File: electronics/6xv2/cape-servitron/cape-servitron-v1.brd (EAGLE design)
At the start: 158.8 x 147.3 mm, 104 parts, among them IC1 74541PW, IC2 74541PW, IC3 74541PW, IC4 LM2574M-5.0, M0-CONN PINHEAD-5MM-1X2, M0-CONN1 PINHEAD-5MM-1X2, M0-CONN2 PINHEAD-5MM-1X2, M0-CONN3 PINHEAD-5MM-1X2, M0-CONN4 PINHEAD-5MM-1X2, M0-CONN5 PINHEAD-5MM-1X2, Q1 BSS123

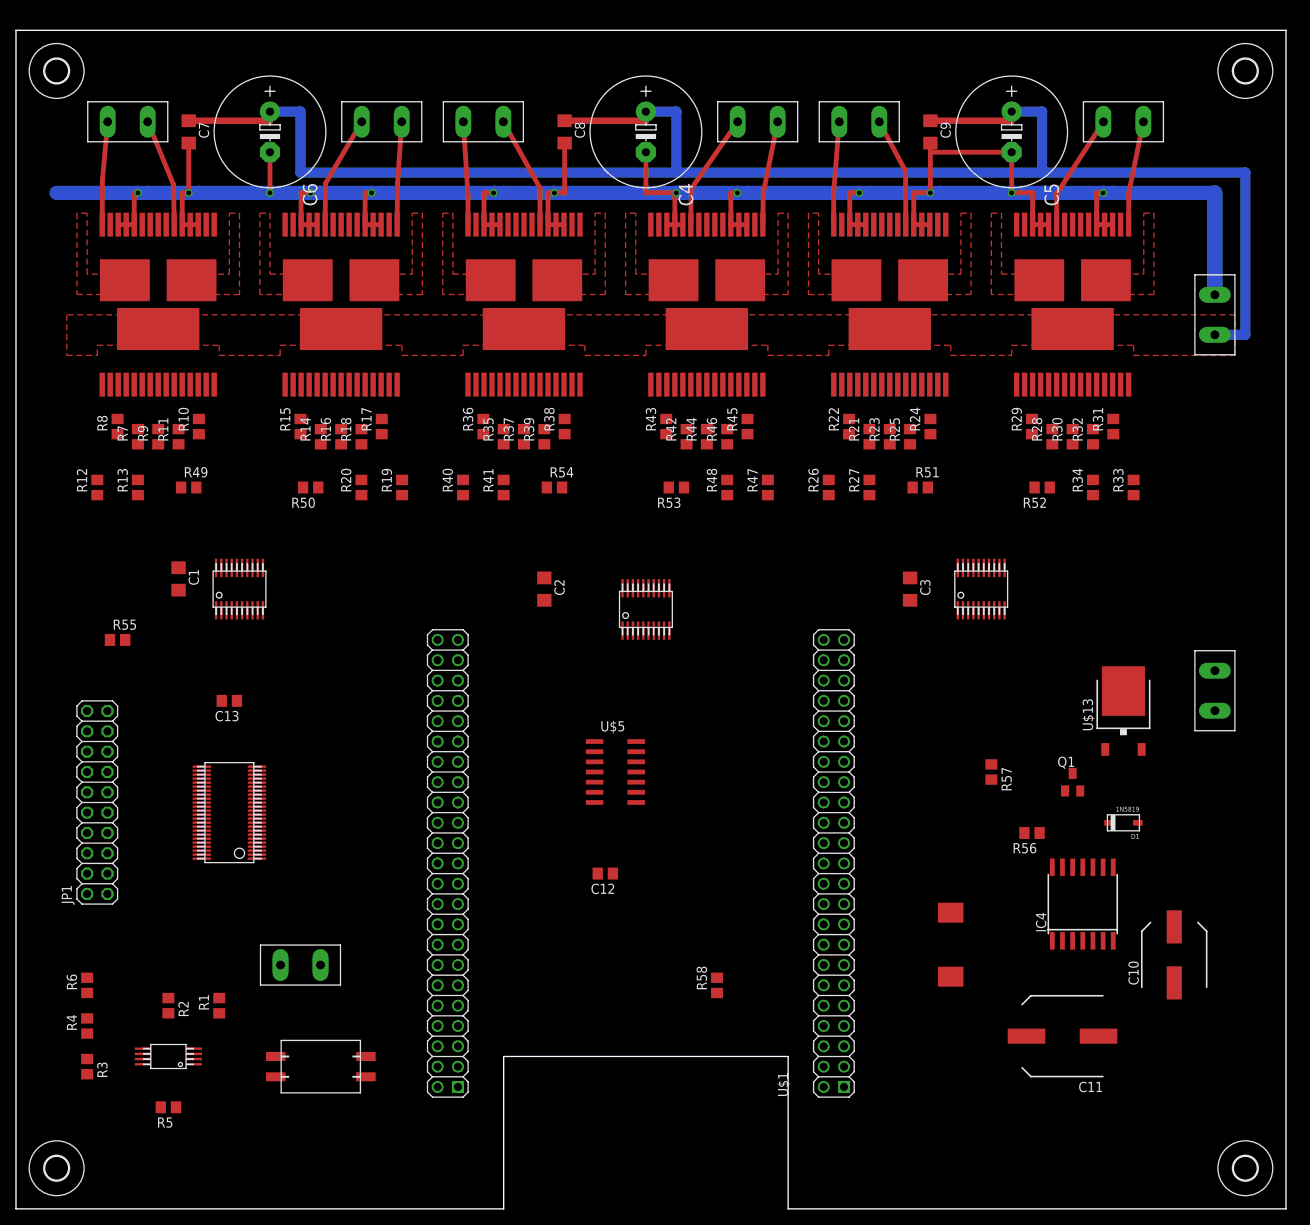
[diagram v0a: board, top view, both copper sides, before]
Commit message: added more heat sinking
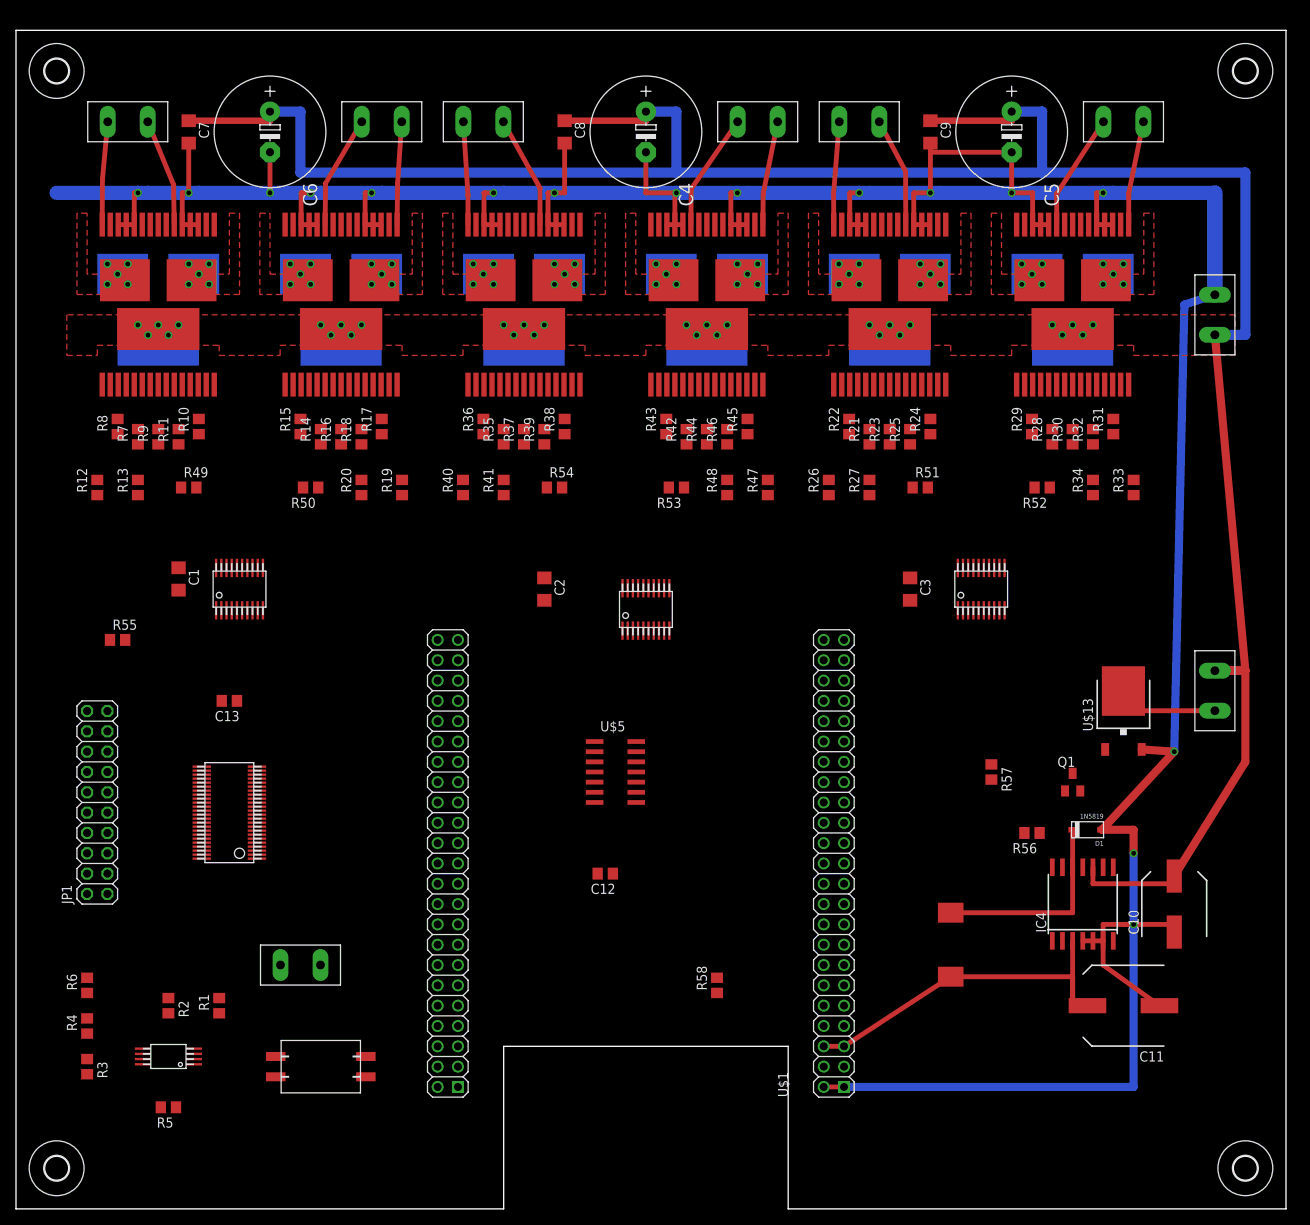
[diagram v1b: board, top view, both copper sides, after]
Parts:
- moved C11 8.52 mm to (138.4, 25.4)
- moved C10 6.35 mm to (144.8, 38.1)
- moved D1 4.56 mm to (133.9, 47.4)
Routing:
- net GND: track 308.9 -> 488.5 mm, vias 13 -> 16
- net +24V: track 210.4 -> 301.6 mm
- net VCC: track 0.00 -> 47.3 mm
- net N$26: track 0.00 -> 25.7 mm
- net N$27: track 0.00 -> 13.9 mm
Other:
- outline, holes or cut-outs redrawn

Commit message: board sent out; cleaning up quadrature assembly
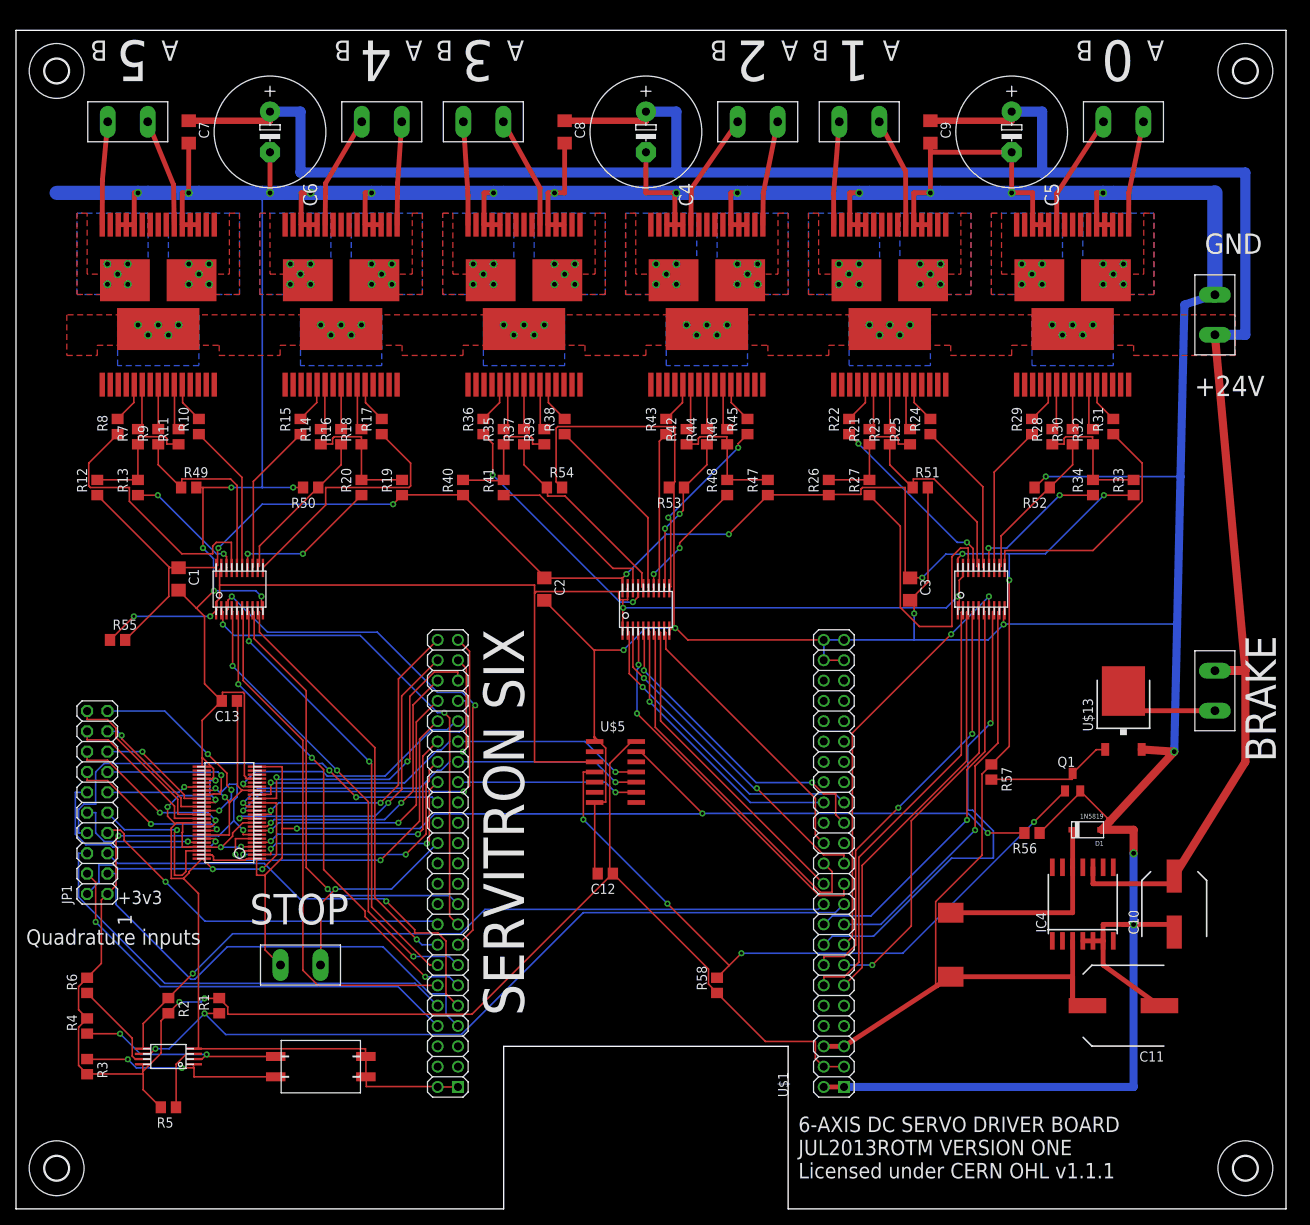
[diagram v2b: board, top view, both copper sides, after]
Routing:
- net GND: track 488.5 -> 980.2 mm, vias 16 -> 33
- net VCC: track 47.3 -> 283.1 mm, vias 0 -> 8
- net +3V3: track 0.00 -> 233.8 mm, vias 0 -> 6
- net !MALL-EN: track 0.00 -> 155.5 mm, vias 0 -> 4
- net EN_BUFFERS: track 0.00 -> 146.4 mm, vias 0 -> 3
- net I2C2_SCL: track 0.00 -> 99.4 mm, vias 0 -> 2
- net I2C2_SDA: track 0.00 -> 94.4 mm, vias 0 -> 1
- net BRAKE: track 0.00 -> 86.3 mm, vias 0 -> 4
- net M0-A: track 0.00 -> 68.9 mm, vias 0 -> 2
- net M1-EN: track 0.00 -> 65.8 mm
- net M0-EN: track 0.00 -> 61.3 mm, vias 0 -> 2
- net M0-B: track 0.00 -> 60.1 mm, vias 0 -> 3
- net M3-PWM: track 0.00 -> 59.7 mm, vias 0 -> 1
- net Q0-A: track 0.00 -> 58.8 mm
- net M0-PWM: track 0.00 -> 58.7 mm, vias 0 -> 3
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- added copper zone on layer 16, net +24V
- added copper zone on layer 16, net OUT0A
- added copper zone on layer 16, net OUT0B
- added copper zone on layer 16, net OUT1A
- added copper zone on layer 16, net OUT1B
- added copper zone on layer 16, net OUT2A
- added copper zone on layer 16, net OUT2B
- added copper zone on layer 16, net OUT3A
- added copper zone on layer 16, net OUT3B
- added copper zone on layer 16, net OUT4A
- added copper zone on layer 16, net OUT4B
- added copper zone on layer 16, net OUT5A
- added copper zone on layer 16, net OUT5B
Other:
- board text added: "+24V"
- board text added: "+3v3"
- board text added: "0"
- board text added: "1"
- board text added: "2"
- board text added: "3"
- board text added: "4"
- board text added: "5"
- board text added: "6-AXIS DC SERVO DRIVER BOARD JUL2013ROTM VERSION ONE Licensed under CERN OHL v1.1.1"
- board text added: "A"
- board text added: "B"
- board text added: "BRAKE"
- board text added: "GND"
- board text added: "Quadrature inputs"
- board text added: "SERVITRON SIX"
- board text added: "STOP"

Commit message: renamed chips and output signals to match board placement and markings
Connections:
- net OUT0A renamed OUT-5B
- net OUT0B renamed OUT-5A
- net OUT1A renamed OUT-4B
- net OUT1B renamed OUT-4A
- net OUT2A renamed OUT-1B
- net OUT2B renamed OUT-1A
- net OUT3A renamed OUT-0B
- net OUT3B renamed OUT-0A
- net OUT4A renamed OUT-3B
- net OUT4B renamed OUT-3A
- net OUT5A renamed OUT-2B
- net OUT5B renamed OUT-2A
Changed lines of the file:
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@@
 <wire x1="15.2908" y1="95.6564" x2="15.24" y2="95.57" width="0.2032" layer="1"/>
 </signal>
-<signal name="OUT0A" class="1">
+<signal name="OUT-5B" class="1">
 <contactref element="U$6" pad="P$1" route="any" routetag="OUT_A"/>
 <contactref element="U$6" pad="P$25" route="any" routetag="OUT_A"/>
@@
 </polygon>
 </signal>
-<signal name="OUT0B" class="1">
+<signal name="OUT-5A" class="1">
 <contactref element="U$6" pad="P$15" route="any" routetag="OUT_B"/>
 <contactref element="U$6" pad="P$16" route="any" routetag="OUT_B"/>
@@
 <wire x1="43.2308" y1="91.1352" x2="43.18" y2="91.12" width="0.2032" layer="1"/>
 </signal>
-<signal name="OUT1A" class="1">
+<signal name="OUT-4B" class="1">
 <contactref element="U$7" pad="P$1" route="any" routetag="OUT_A"/>
 <contactref element="U$7" pad="P$25" route="any" routetag="OUT_A"/>
@@
 </polygon>
 </signal>
-<signal name="OUT1B" class="1">
+<signal name="OUT-4A" class="1">
 <contactref element="U$7" pad="P$15" route="any" routetag="OUT_B"/>
 <contactref element="U$7" pad="P$16" route="any" routetag="OUT_B"/>
@@
 <wire x1="106.7308" y1="95.6564" x2="106.68" y2="95.57" width="0.2032" layer="1"/>
 </signal>
-<signal name="OUT2A" class="1">
+<signal name="OUT-1B" class="1">
 <contactref element="U$8" pad="P$1" route="any" routetag="OUT_A"/>
 <contactref element="U$8" pad="P$25" route="any" routetag="OUT_A"/>
@@
 </polygon>
 </signal>
-<signal name="OUT2B" class="1">
+<signal name="OUT-1A" class="1">
 <contactref element="U$8" pad="P$15" route="any" routetag="OUT_B"/>
 <contactref element="U$8" pad="P$16" route="any" routetag="OUT_B"/>
@@
 <wire x1="134.6708" y1="91.1352" x2="134.62" y2="91.12" width="0.2032" layer="1"/>
 </signal>
-<signal name="OUT3A" class="1">
+<signal name="OUT-0B" class="1">
 <contactref element="U$9" pad="P$1" route="any" routetag="OUT_A"/>
 <contactref element="U$9" pad="P$25" route="any" routetag="OUT_A"/>
@@
 </polygon>
 </signal>
-<signal name="OUT3B" class="1">
+<signal name="OUT-0A" class="1">
 <contactref element="U$9" pad="P$15" route="any" routetag="OUT_B"/>
 <contactref element="U$9" pad="P$16" route="any" routetag="OUT_B"/>
@@
 <wire x1="61.0108" y1="95.6564" x2="60.96" y2="95.57" width="0.2032" layer="1"/>
 </signal>
-<signal name="OUT4A" class="1">
+<signal name="OUT-3B" class="1">
 <contactref element="U$10" pad="P$1" route="any" routetag="OUT_A"/>
 <contactref element="U$10" pad="P$25" route="any" routetag="OUT_A"/>
@@
 </polygon>
 </signal>
-<signal name="OUT4B" class="1">
+<signal name="OUT-3A" class="1">
 <contactref element="U$10" pad="P$15" route="any" routetag="OUT_B"/>
 <contactref element="U$10" pad="P$16" route="any" routetag="OUT_B"/>
@@
 <wire x1="88.9508" y1="91.1352" x2="88.9" y2="91.12" width="0.2032" layer="1"/>
 </signal>
-<signal name="OUT5A" class="1">
+<signal name="OUT-2B" class="1">
 <contactref element="U$11" pad="P$1" route="any" routetag="OUT_A"/>
 <contactref element="U$11" pad="P$25" route="any" routetag="OUT_A"/>
@@
 </polygon>
 </signal>
-<signal name="OUT5B" class="1">
+<signal name="OUT-2A" class="1">
 <contactref element="U$11" pad="P$15" route="any" routetag="OUT_B"/>
 <contactref element="U$11" pad="P$16" route="any" routetag="OUT_B"/>

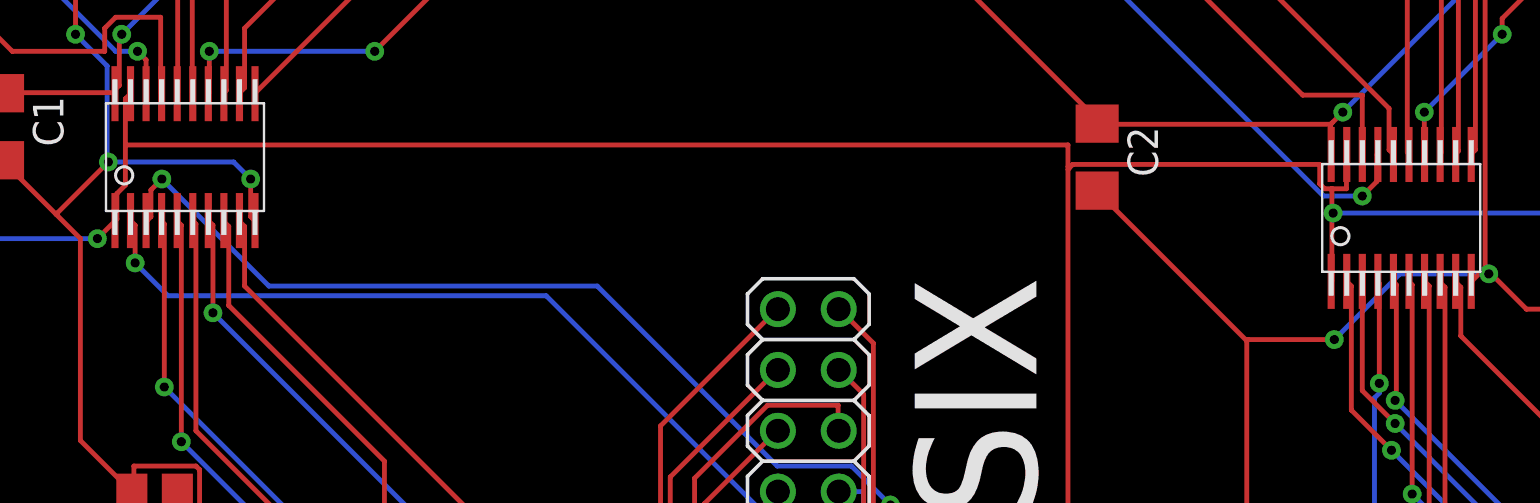
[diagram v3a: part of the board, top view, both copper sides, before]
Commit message: updated signals for current layout
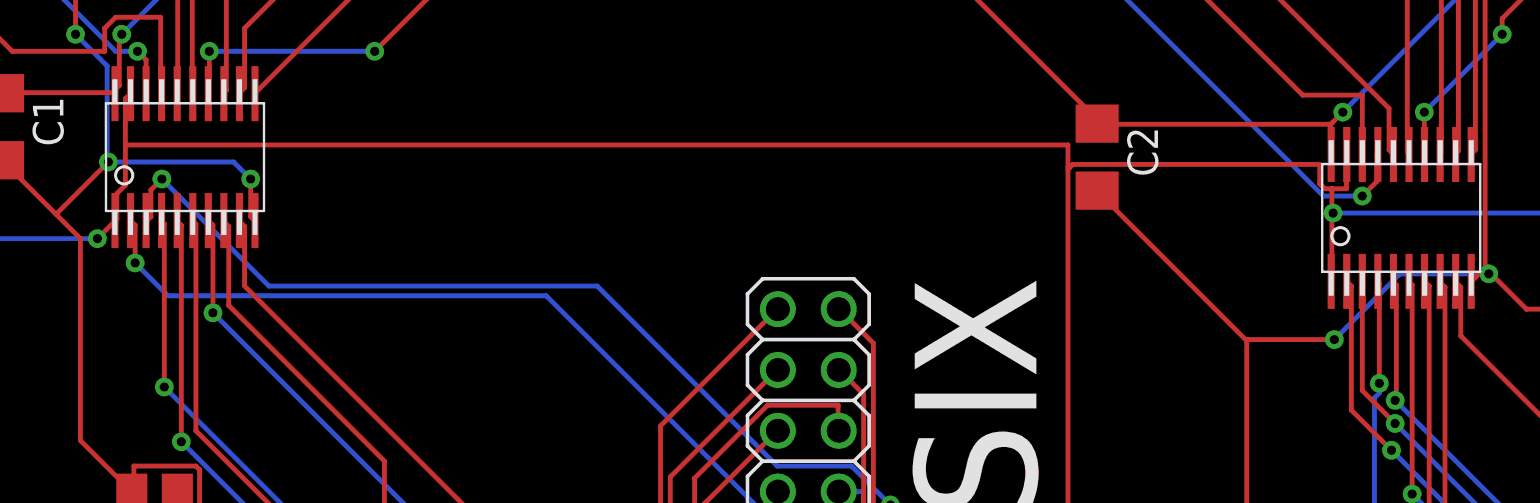
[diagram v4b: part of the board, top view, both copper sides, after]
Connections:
- net M0-A renamed M5_B
- net M0-B renamed M5_A
- net M0-EN renamed M5_EN
- net M0-PWM renamed M5_PWM
- net M1-A renamed M4_B
- net M1-B renamed M4_A
- net M1-EN renamed M4_EN
- net M1-PWM renamed M4_PWM
- net M2-A renamed M1_B
- net M2-B renamed M1_A
- net M2-EN renamed M1_EN
- net M2-PWM renamed M1_PWM
- net M3-A renamed M0_B
- net M3-B renamed M0_A
- net M3-EN renamed M0_EN
- net M3-PWM renamed M0_PWM
- net M4-A renamed M3_B
- net M4-B renamed M3_A
- net M4-EN renamed M3_EN
- net M4-PWM renamed M3_PWM
- net M5-A renamed M2_B
- net M5-B renamed M2_A
- net M5-EN renamed M2_EN
- net M5-PWM renamed M2_PWM
